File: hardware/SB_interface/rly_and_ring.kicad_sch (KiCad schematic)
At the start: 17 parts, among them K5 J104D2C12VDC.36S, Q11 MMBTA42, Q12 MMBTA42, Q13 2N7002

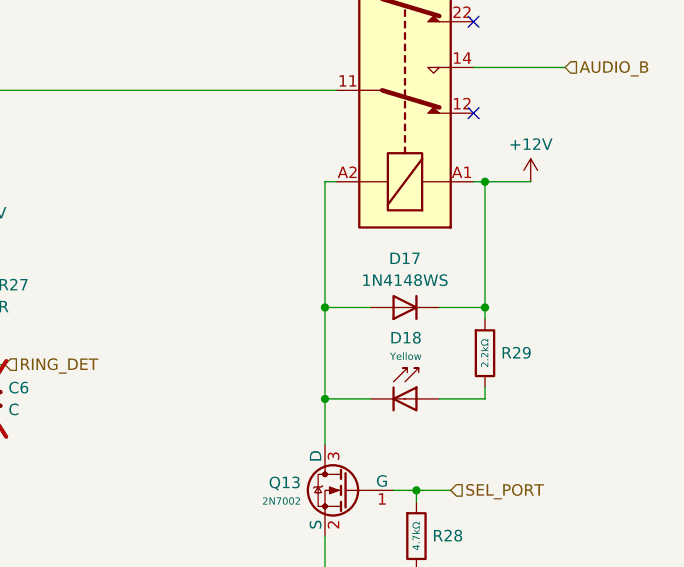
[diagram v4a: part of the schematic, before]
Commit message: added prototyping area
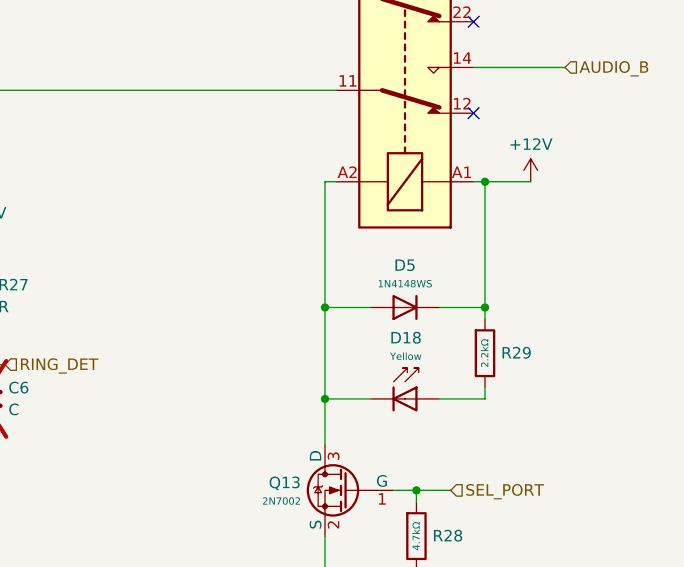
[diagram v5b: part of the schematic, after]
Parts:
- removed D17: 1N4148WS, Diode_SMD:D_SOD-323, symbol Diode:1N4148WS
- added D5: 1N4148WS, PCM_JLCPCB:D_SOD-323, symbol PCM_JLCPCB-Diodes:Switching,1N4148WS
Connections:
- net +12V: now also D5.1
- net at D18.1, K5.A2, Q13.3 (D): now also D5.2
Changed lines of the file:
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@@
+	)
+	(symbol
+		(lib_id "PCM_JLCPCB-Diodes:Switching,1N4148WS")
+		(at 130.81 62.23 90)
+		(unit 1)
+		(exclude_from_sim no)
+		(in_bom yes)
+		(on_board yes)
+		(dnp no)
+		(fields_autoplaced yes)
+		(property "Reference" "D5"
+			(at 130.81 57.5719 90)
+			(effects
+				(font
+					(size 1.27 1.27)
+				)
+			)
+		)
+		(property "Value" "1N4148WS"
+			(at 130.81 59.6181 90)
+			(effects
+				(font
+					(size 0.8 0.8)
+				)
+			)
+		)
+		(property "Footprint" "PCM_JLCPCB:D_SOD-323"
+			(at 130.81 64.008 90)
+			(effects
+				(font
+					(size 1.27 1.27)
+				)
+				(hide yes)
+			)
+		)
+		(property "Datasheet" "https://www.lcsc.com/datasheet/lcsc_datasheet_1810101110_Jiangsu-Changjing-Electronics-Technology-Co---Ltd--1N4148WS_C2128.pdf"
+			(at 130.81 62.23 0)
+			(effects
+				(font
+					(size 1.27 1.27)
+				)
+				(hide yes)
+			)
+		)
+		(property "Description" "100V Independent Type 1.25V@150mA 4ns 150mA SOD-323 Switching Diodes ROHS"
+			(at 130.81 62.23 0)
+			(effects
+				(font
+					(size 1.27 1.27)
+				)
+				(hide yes)
+			)
+		)
+		(property "LCSC" "C2128"
+			(at 130.81 62.23 0)
+			(effects
+				(font
+					(size 1.27 1.27)
+				)
+				(hide yes)
+			)
+		)
+		(property "Stock" "2886910"
+			(at 130.81 62.23 0)
+			(effects
+				(font
+					(size 1.27 1.27)
+				)
+				(hide yes)
+			)
+		)
+		(property "Price" "0.012USD"
+			(at 130.81 62.23 0)
+			(effects
+				(font
+					(size 1.27 1.27)
+				)
+				(hide yes)
+			)
+		)
+		(property "Process" "SMT"
+			(at 130.81 62.23 0)
+			(effects
+				(font
+					(size 1.27 1.27)
+				)
+				(hide yes)
+			)
+		)
+		(property "Minimum Qty" "20"
+			(at 130.81 62.23 0)
+			(effects
+				(font
+					(size 1.27 1.27)
+				)
+				(hide yes)
+			)
+		)
+		(property "Attrition Qty" "10"
+			(at 130.81 62.23 0)
+			(effects
+				(font
+					(size 1.27 1.27)
+				)
+				(hide yes)
+			)
+		)
+		(property "Class" "Basic Component"
+			(at 130.81 62.23 0)
+			(effects
+				(font
+					(size 1.27 1.27)
+				)
+				(hide yes)
+			)
+		)
+		(property "Category" "Diodes,Switching Diode"
+			(at 130.81 62.23 0)
+			(effects
+				(font
+					(size 1.27 1.27)
+				)
+				(hide yes)
+			)
+		)
+		(property "Manufacturer" "Changjiang Electronics Tech (CJ)"
+			(at 130.81 62.23 0)
+			(effects
+				(font
+					(size 1.27 1.27)
+				)
+				(hide yes)
+			)
+		)
+		(property "Part" "1N4148WS"
+			(at 130.81 62.23 0)
+			(effects
+				(font
+					(size 1.27 1.27)
+				)
+				(hide yes)
+			)
+		)
+		(property "Rectified Current" "150mA"
+			(at 130.81 62.23 0)
+			(effects
+				(font
+					(size 1.27 1.27)
+				)
+				(hide yes)
+			)
+		)
+		(property "Forward Voltage (Vf@If)" "1.25V@150mA"
+			(at 130.81 62.23 0)
+			(effects
+				(font
+					(size 1.27 1.27)
+				)
+				(hide yes)
+			)
+		)
+		(property "Reverse Voltage (Vr)" "100V"
+			(at 130.81 62.23 0)
+			(effects
+				(font
+					(size 1.27 1.27)
+				)
+				(hide yes)
+			)
+		)
+		(property "Reverse Recovery Time (trr)" "4ns"
+			(at 130.81 62.23 0)
+			(effects
+				(font
+					(size 1.27 1.27)
+				)
+				(hide yes)
+			)
+		)
+		(property "Diode Configuration" "Independent Type"
+			(at 130.81 62.23 0)
+			(effects
+				(font
+					(size 1.27 1.27)
+				)
+				(hide yes)
+			)
+		)
+		(property "Reverse Leakage Current" "1uA@75V"
+			(at 130.81 62.23 0)
+			(effects
+				(font
+					(size 1.27 1.27)
+				)
+				(hide yes)
+			)
+		)
+		(pin "1"
+		)
+		(pin "2"
+		)
+		(instances
+			(project "SB_interface"
+				(path "/4cb02b16-1366-401e-b585-6b8c16ca1e0c/04da6c3e-f142-4424-9ae7-5f4ad80b9e64"
+					(reference "D17")
+					(unit 1)
+				)
+				(path "/4cb02b16-1366-401e-b585-6b8c16ca1e0c/4c455e0f-2f75-44d8-9351-ac4c17de5403"
+					(reference "D13")
+					(unit 1)
+				)
+				(path "/4cb02b16-1366-401e-b585-6b8c16ca1e0c/4d2fead3-b87b-4542-a4c7-733f85ed8b2b"
+					(reference "D21")
+					(unit 1)
+				)
+				(path "/4cb02b16-1366-401e-b585-6b8c16ca1e0c/5a87cade-2221-4272-9aac-ffd7b503276a"
+					(reference "D29")
+					(unit 1)
+				)
+				(path "/4cb02b16-1366-401e-b585-6b8c16ca1e0c/65f428e1-6254-4cfe-ba3e-d888b98d881a"
+					(reference "D49")
+					(unit 1)
+				)
+				(path "/4cb02b16-1366-401e-b585-6b8c16ca1e0c/68f1488c-50b9-4246-a0ed-d62d33bd08f7"
+					(reference "D5")
+					(unit 1)
+				)
+				(path "/4cb02b16-1366-401e-b585-6b8c16ca1e0c/718ce444-f032-46dc-bc79-6b4c8de558e5"
+					(reference "D45")
+					(unit 1)
+				)
+				(path "/4cb02b16-1366-401e-b585-6b8c16ca1e0c/7b371750-1eb6-4f54-9083-3d5e67feee11"
+					(reference "D41")
+					(unit 1)
+				)
+				(path "/4cb02b16-1366-401e-b585-6b8c16ca1e0c/7beaa6f4-34b4-4c80-91ce-5a7475c86d6e"
+					(reference "D33")
+					(unit 1)
+				)
+				(path "/4cb02b16-1366-401e-b585-6b8c16ca1e0c/b0d52d74-3991-41e9-96d0-192dcb3ea05c"
+					(reference "D37")
+					(unit 1)
+				)
+				(path "/4cb02b16-1366-401e-b585-6b8c16ca1e0c/bc1d0a00-a3b6-43d8-9a36-6cd9b07e4047"
+					(reference "D25")
+					(unit 1)
+				)
+				(path "/4cb02b16-1366-401e-b585-6b8c16ca1e0c/cd5bf1ca-4913-499a-ad95-a6efc522edaf"
+					(reference "D9")
+					(unit 1)
+				)
+			)
+		)
 	)
 	(symbol
@@
 					(unit 1)
 				)
-			)
-		)
-	)
-	(symbol
-		(lib_id "Diode:1N4148WS")
-		(at 130.81 62.23 180)
-		(unit 1)
-		(exclude_from_sim no)
-		(in_bom yes)
-		(on_board yes)
-		(dnp no)
-		(fields_autoplaced yes)
-		(property "Reference" "D17"
-			(at 130.81 56.8155 0)
-			(effects
-				(font
-					(size 1.27 1.27)
-				)
-			)
-		)
-		(property "Value" "1N4148WS"
-			(at 130.81 59.2398 0)
-			(effects
-				(font
-					(size 1.27 1.27)
-				)
-			)
-		)
-		(property "Footprint" "Diode_SMD:D_SOD-323"
-			(at 130.81 57.785 0)
-			(effects
-				(font
-					(size 1.27 1.27)
-				)
-				(hide yes)
-			)
-		)
-		(property "Datasheet" "https://www.vishay.com/docs/85751/1n4148ws.pdf"
-			(at 130.81 62.23 0)
-			(effects
-				(font
-					(size 1.27 1.27)
-				)
-				(hide yes)
-			)
-		)
-		(property "Description" "75V 0.15A Fast switching Diode, SOD-323"
-			(at 130.81 62.23 0)
-			(effects
-				(font
-					(size 1.27 1.27)
-				)
-				(hide yes)
-			)
-		)
-		(property "Sim.Device" "D"
-			(at 130.81 62.23 0)
-			(effects
-				(font
-					(size 1.27 1.27)
-				)
-				(hide yes)
-			)
-		)
-		(property "Sim.Pins" "1=K 2=A"
-			(at 130.81 62.23 0)
-			(effects
-				(font
-					(size 1.27 1.27)
-				)
-				(hide yes)
-			)
-		)
-		(pin "2"
-		)
-		(pin "1"
-		)
-		(instances
-			(project "SB_interface"
-				(path "/4cb02b16-1366-401e-b585-6b8c16ca1e0c/04da6c3e-f142-4424-9ae7-5f4ad80b9e64"
-					(reference "D17")
-					(unit 1)
-				)
-				(path "/4cb02b16-1366-401e-b585-6b8c16ca1e0c/4c455e0f-2f75-44d8-9351-ac4c17de5403"
-					(reference "D13")
-					(unit 1)
-				)
-				(path "/4cb02b16-1366-401e-b585-6b8c16ca1e0c/4d2fead3-b87b-4542-a4c7-733f85ed8b2b"
-					(reference "D21")
-					(unit 1)
-				)
-				(path "/4cb02b16-1366-401e-b585-6b8c16ca1e0c/5a87cade-2221-4272-9aac-ffd7b503276a"
-					(reference "D29")
-					(unit 1)
-				)
-				(path "/4cb02b16-1366-401e-b585-6b8c16ca1e0c/65f428e1-6254-4cfe-ba3e-d888b98d881a"
-					(reference "D49")
-					(unit 1)
-				)
-				(path "/4cb02b16-1366-401e-b585-6b8c16ca1e0c/68f1488c-50b9-4246-a0ed-d62d33bd08f7"
-					(reference "D5")
-					(unit 1)
-				)
-				(path "/4cb02b16-1366-401e-b585-6b8c16ca1e0c/718ce444-f032-46dc-bc79-6b4c8de558e5"
-					(reference "D45")
-					(unit 1)
-				)
-				(path "/4cb02b16-1366-401e-b585-6b8c16ca1e0c/7b371750-1eb6-4f54-9083-3d5e67feee11"
-					(reference "D41")
-					(unit 1)
-				)
-				(path "/4cb02b16-1366-401e-b585-6b8c16ca1e0c/7beaa6f4-34b4-4c80-91ce-5a7475c86d6e"
-					(reference "D33")
-					(unit 1)
-				)
-				(path "/4cb02b16-1366-401e-b585-6b8c16ca1e0c/b0d52d74-3991-41e9-96d0-192dcb3ea05c"
-					(reference "D37")
-					(unit 1)
-				)
-				(path "/4cb02b16-1366-401e-b585-6b8c16ca1e0c/bc1d0a00-a3b6-43d8-9a36-6cd9b07e4047"
-					(reference "D25")
-					(unit 1)
-				)
-				(path "/4cb02b16-1366-401e-b585-6b8c16ca1e0c/cd5bf1ca-4913-499a-ad95-a6efc522edaf"
-					(reference "D9")
-					(unit 1)
-				)
